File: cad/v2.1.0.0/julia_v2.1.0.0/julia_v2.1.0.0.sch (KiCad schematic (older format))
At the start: 0 parts

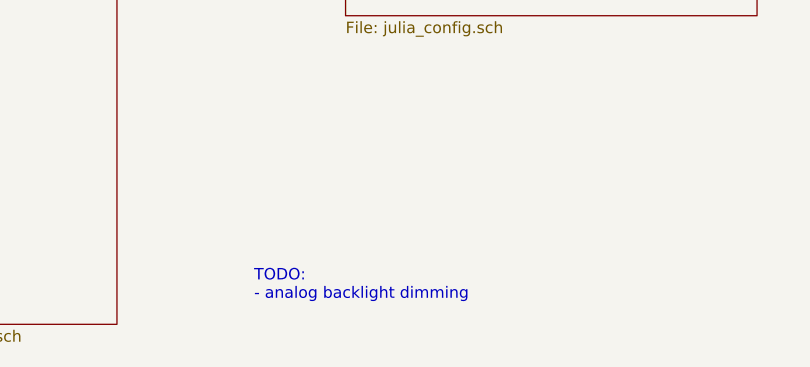
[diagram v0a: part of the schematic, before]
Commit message: v2.1.0.0: changed connector, ERC, annotation/footprint assignment
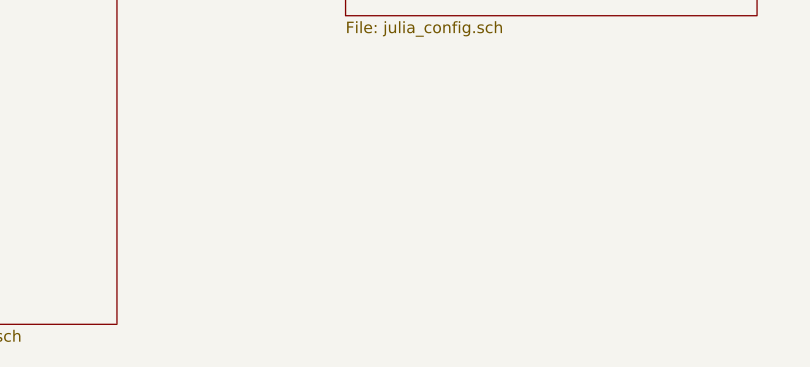
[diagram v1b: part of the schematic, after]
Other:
- note removed: "TODO:\n- analog backlight dimming"
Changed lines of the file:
@@
 F12 "SCL" I R 3200 5800 50
 $EndSheet
-Text Notes 5700 5800 0    50   ~ 0
-TODO:\n- analog backlight dimming
 $Sheet
 S 1650 2600 1550 1500
